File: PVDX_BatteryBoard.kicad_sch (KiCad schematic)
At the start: 5 parts

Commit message: connectors
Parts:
- removed Rt1: 16.121k, symbol Device:R_US
- removed Rt2: 5.993k, symbol Device:R_US
- removed TH1: Thermistor_NTC_US, Thermistor_NXFT15XV103FEAB025:Thermistor_ NXFT15XV103FEAB025, symbol Device:Thermistor_NTC_US
- renumbered Rh to thermistor_high_temp, Rl to thermistor_low_temp
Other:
- added sheet Boards (PVDX_BatteryBoard_Board.kicad_sch)
- added sheet Connectors (PVDX_BatteryBoard_connectors.kicad_sch)
- note added: "for reference only"
- note added: "input connector (5V in from eps, heater_on signal for heaters)"
- moved on the sheet: thermistor_high_temp, thermistor_low_temp
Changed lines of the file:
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@@
 	(generator_version "9.0")
 	(paper "A4")
-	(symbol
-		(lib_id "Device:Thermistor_NTC_US")
-		(at 95.25 77.47 0)
-		(unit 1)
-		(exclude_from_sim no)
-		(in_bom yes)
-		(on_board yes)
-		(dnp no)
-		(fields_autoplaced yes)
-		(property "Reference" "TH1"
-			(at 97.79 76.5174 0)
-			(effects
-				(font
-					(size 1.27 1.27)
-				)
-				(justify left)
-			)
-		)
-		(property "Value" "Thermistor_NTC_US"
-			(at 97.79 79.0574 0)
-			(effects
-				(font
-					(size 1.27 1.27)
-				)
-				(justify left)
-			)
-		)
-		(property "Footprint" "Thermistor_NXFT15XV103FEAB025:Thermistor_ NXFT15XV103FEAB025"
-			(at 95.25 76.2 0)
-			(effects
-				(font
-					(size 1.27 1.27)
-				)
-				(hide yes)
-			)
-		)
-		(property "Datasheet" "~"
-			(at 95.25 76.2 0)
-			(effects
-				(font
-					(size 1.27 1.27)
-				)
-				(hide yes)
-			)
-		)
-		(property "Description" "Temperature dependent resistor, negative temperature coefficient, US symbol"
-			(at 95.25 77.47 0)
-			(effects
-				(font
-					(size 1.27 1.27)
-				)
-				(hide yes)
-			)
-		)
-		(pin "2"
-		)
-		(pin "1"
-		)
-		(instances
-			(project ""
-				(path "/c318761a-e6d3-4e59-aaa2-0d170bce7cde"
-					(reference "TH1")
-					(unit 1)
-				)
+	(rectangle
+		(start 139.7 97.79)
+		(end 198.12 119.38)
+		(stroke
+			(width 0)
+			(type default)
+		)
+		(fill
+			(type none)
+		)
+	)
+	(text "input connector (5V in from eps, heater_on signal for heaters)"
+		(exclude_from_sim no)
+		(at 100.584 131.064 0)
+		(effects
+			(font
+				(size 1.27 1.27)
+			)
+		)
+	)
+	(text "for reference only"
+		(exclude_from_sim no)
+		(at 163.576 113.792 0)
+		(effects
+			(font
+				(size 1.27 1.27)
 			)
 		)
@@
 	(symbol
 		(lib_id "Device:R_US")
-		(at 151.13 81.28 0)
+		(at 144.78 106.68 0)
 		(unit 1)
 		(exclude_from_sim no)
@@
 		(dnp no)
 		(fields_autoplaced yes)
-		(property "Reference" "Rt2"
-			(at 153.67 80.0099 0)
-			(effects
-				(font
-					(size 1.27 1.27)
-				)
-				(justify left)
-			)
-		)
-		(property "Value" "5.993k"
-			(at 153.67 82.5499 0)
+		(property "Reference" "thermistor_high_temp"
+			(at 147.32 105.4099 0)
+			(effects
+				(font
+					(size 1.27 1.27)
+				)
+				(justify left)
+			)
+		)
+		(property "Value" "2.498k"
+			(at 147.32 107.9499 0)
 			(effects
 				(font
@@
 		)
 		(property "Footprint" ""
-			(at 152.146 81.534 90)
+			(at 145.796 106.934 90)
 			(effects
 				(font
@@
 		)
 		(property "Datasheet" "~"
-			(at 151.13 81.28 0)
+			(at 144.78 106.68 0)
 			(effects
 				(font
@@
 		)
 		(property "Description" "Resistor, US symbol"
-			(at 151.13 81.28 0)
-			(effects
-				(font
-					(size 1.27 1.27)
-				)
-				(hide yes)
-			)
+			(at 144.78 106.68 0)
+			(effects
+				(font
+					(size 1.27 1.27)
+				)
+				(hide yes)
+			)
+		)
+		(pin "1"
 		)
 		(pin "2"
 		)
-		(pin "1"
-		)
 		(instances
 			(project ""
 				(path "/c318761a-e6d3-4e59-aaa2-0d170bce7cde"
-					(reference "Rt2")
+					(reference "thermistor_high_temp")
 					(unit 1)
 				)
@@
 	(symbol
 		(lib_id "Device:R_US")
-		(at 137.16 81.28 0)
+		(at 172.72 107.95 0)
 		(unit 1)
 		(exclude_from_sim no)
@@
 		(dnp no)
 		(fields_autoplaced yes)
-		(property "Reference" "Rt1"
-			(at 139.7 80.0099 0)
-			(effects
-				(font
-					(size 1.27 1.27)
-				)
-				(justify left)
-			)
-		)
-		(property "Value" "16.121k"
-			(at 139.7 82.5499 0)
+		(property "Reference" "thermistor_low_temp"
+			(at 175.26 106.6799 0)
+			(effects
+				(font
+					(size 1.27 1.27)
+				)
+				(justify left)
+			)
+		)
+		(property "Value" "33.476k"
+			(at 175.26 109.2199 0)
 			(effects
 				(font
@@
 		)
 		(property "Footprint" ""
-			(at 138.176 81.534 90)
+			(at 173.736 108.204 90)
 			(effects
 				(font
@@
 		)
 		(property "Datasheet" "~"
-			(at 137.16 81.28 0)
+			(at 172.72 107.95 0)
 			(effects
 				(font
@@
 		)
 		(property "Description" "Resistor, US symbol"
-			(at 137.16 81.28 0)
-			(effects
-				(font
-					(size 1.27 1.27)
-				)
-				(hide yes)
-			)
+			(at 172.72 107.95 0)
+			(effects
+				(font
+					(size 1.27 1.27)
+				)
+				(hide yes)
+			)
+		)
+		(pin "2"
 		)
 		(pin "1"
 		)
-		(pin "2"
-		)
 		(instances
 			(project ""
 				(path "/c318761a-e6d3-4e59-aaa2-0d170bce7cde"
-					(reference "Rt1")
+					(reference "thermistor_low_temp")
 					(unit 1)
 				)
@@
 		)
 	)
-	(symbol
-		(lib_id "Device:R_US")
-		(at 111.76 104.14 0)
-		(unit 1)
-		(exclude_from_sim no)
-		(in_bom yes)
-		(on_board yes)
-		(dnp no)
-		(fields_autoplaced yes)
-		(property "Reference" "Rh"
-			(at 114.3 102.8699 0)
-			(effects
-				(font
-					(size 1.27 1.27)
-				)
-				(justify left)
-			)
-		)
-		(property "Value" "2.498k"
-			(at 114.3 105.4099 0)
-			(effects
-				(font
-					(size 1.27 1.27)
-				)
-				(justify left)
-			)
-		)
-		(property "Footprint" ""
-			(at 112.776 104.394 90)
-			(effects
-				(font
-					(size 1.27 1.27)
-				)
-				(hide yes)
-			)
-		)
-		(property "Datasheet" "~"
-			(at 111.76 104.14 0)
-			(effects
-				(font
-					(size 1.27 1.27)
-				)
-				(hide yes)
-			)
-		)
-		(property "Description" "Resistor, US symbol"
-			(at 111.76 104.14 0)
-			(effects
-				(font
-					(size 1.27 1.27)
-				)
-				(hide yes)
-			)
-		)
-		(pin "1"
-		)
-		(pin "2"
-		)
-		(instances
-			(project ""
-				(path "/c318761a-e6d3-4e59-aaa2-0d170bce7cde"
-					(reference "Rh")
-					(unit 1)
-				)
-			)
-		)
-	)
-	(symbol
-		(lib_id "Device:R_US")
-		(at 88.9 100.33 0)
-		(unit 1)
-		(exclude_from_sim no)
-		(in_bom yes)
-		(on_board yes)
-		(dnp no)
-		(fields_autoplaced yes)
-		(property "Reference" "Rl"
-			(at 91.44 99.0599 0)
-			(effects
-				(font
-					(size 1.27 1.27)
-				)
-				(justify left)
-			)
-		)
-		(property "Value" "33.476k"
-			(at 91.44 101.5999 0)
-			(effects
-				(font
-					(size 1.27 1.27)
-				)
-				(justify left)
-			)
-		)
-		(property "Footprint" ""
-			(at 89.916 100.584 90)
-			(effects
-				(font
-					(size 1.27 1.27)
-				)
-				(hide yes)
-			)
-		)
-		(property "Datasheet" "~"
-			(at 88.9 100.33 0)
-			(effects
-				(font
-					(size 1.27 1.27)
-				)
-				(hide yes)
-			)
-		)
-		(property "Description" "Resistor, US symbol"
-			(at 88.9 100.33 0)
-			(effects
-				(font
-					(size 1.27 1.27)
-				)
-				(hide yes)
-			)
-		)
-		(pin "2"
-		)
-		(pin "1"
-		)
-		(instances
-			(project ""
-				(path "/c318761a-e6d3-4e59-aaa2-0d170bce7cde"
-					(reference "Rl")
-					(unit 1)
-				)
-			)
+	(sheet
+		(at 116.84 57.15)
+		(size 13.97 3.81)
+		(exclude_from_sim no)
+		(in_bom yes)
+		(on_board yes)
+		(dnp no)
+		(fields_autoplaced yes)
+		(stroke
+			(width 0.1524)
+			(type solid)
+		)
+		(fill
+			(color 0 0 0 0.0000)
+		)
+		(property "Sheetname" "Boards"
+			(at 116.84 56.4384 0)
+			(effects
+				(font
+					(size 1.27 1.27)
+				)
+				(justify left bottom)
+			)
+		)
+		(property "Sheetfile" "PVDX_BatteryBoard_Board.kicad_sch"
+			(at 116.84 61.5446 0)
+			(effects
+				(font
+					(size 1.27 1.27)
+				)
+				(justify left top)
+			)
+		)
+		(instances
+			(project "PVDX_BatteryBoard"
+				(path "/c318761a-e6d3-4e59-aaa2-0d170bce7cde"
+					(page "3")
+				)
+			)
+		)
+	)
+	(sheet
+		(at 116.84 46.99)
+		(size 13.97 3.81)
+		(exclude_from_sim no)
+		(in_bom yes)
+		(on_board yes)
+		(dnp no)
+		(fields_autoplaced yes)
+		(stroke
+			(width 0.1524)
+			(type solid)
+		)
+		(fill
+			(color 0 0 0 0.0000)
+		)
+		(property "Sheetname" "Connectors"
+			(at 116.84 46.2784 0)
+			(effects
+				(font
+					(size 1.27 1.27)
+				)
+				(justify left bottom)
+			)
+		)
+		(property "Sheetfile" "PVDX_BatteryBoard_connectors.kicad_sch"
+			(at 116.84 51.3846 0)
+			(effects
+				(font
+					(size 1.27 1.27)
+				)
+				(justify left top)
+			)
+		)
+		(instances
+			(project "PVDX_BatteryBoard"
+				(path "/c318761a-e6d3-4e59-aaa2-0d170bce7cde"
+					(page "2")
+				)
+			)

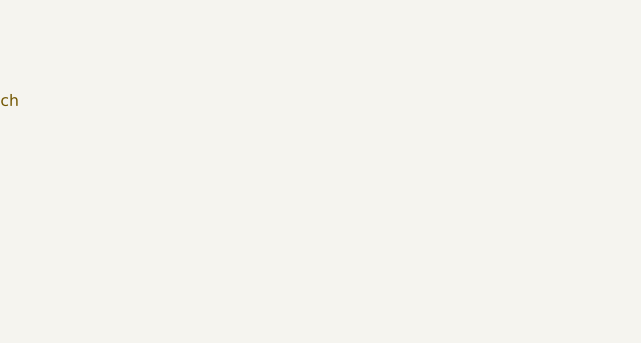
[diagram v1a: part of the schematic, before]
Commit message: added heater schematic
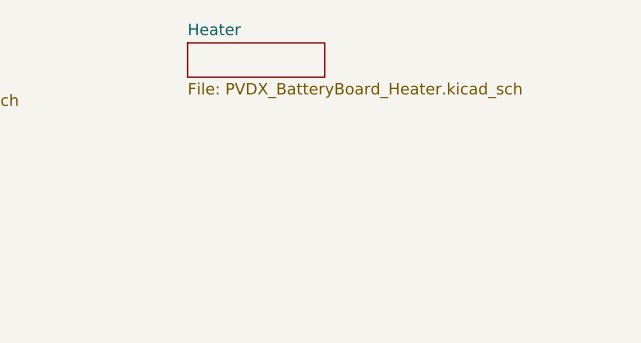
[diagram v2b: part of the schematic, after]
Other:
- added sheet Heater (PVDX_BatteryBoard_Heater.kicad_sch)
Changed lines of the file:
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@@
+	)
+	(sheet
+		(at 176.53 45.72)
+		(size 15.24 3.81)
+		(exclude_from_sim no)
+		(in_bom yes)
+		(on_board yes)
+		(dnp no)
+		(fields_autoplaced yes)
+		(stroke
+			(width 0.1524)
+			(type solid)
+		)
+		(fill
+			(color 0 0 0 0.0000)
+		)
+		(property "Sheetname" "Heater"
+			(at 176.53 45.0084 0)
+			(effects
+				(font
+					(size 1.27 1.27)
+				)
+				(justify left bottom)
+			)
+		)
+		(property "Sheetfile" "PVDX_BatteryBoard_Heater.kicad_sch"
+			(at 176.53 50.1146 0)
+			(effects
+				(font
+					(size 1.27 1.27)
+				)
+				(justify left top)
+			)
+		)
+		(instances
+			(project "PVDX_BatteryBoard"
+				(path "/c318761a-e6d3-4e59-aaa2-0d170bce7cde"
+					(page "4")
+				)
+			)
+		)
 	)
 	(sheet
